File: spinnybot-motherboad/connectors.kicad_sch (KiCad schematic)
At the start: 9 parts, among them J10 LEDSTRIP3, J11 MOTOR2, J12 MOTOR3, J13 MOTOR1, J5 LEDSTRIP1, J6 LEDSTRIP2, J7 LEDSTRIP3, J8 LEDSTRIP1, J9 LEDSTRIP2

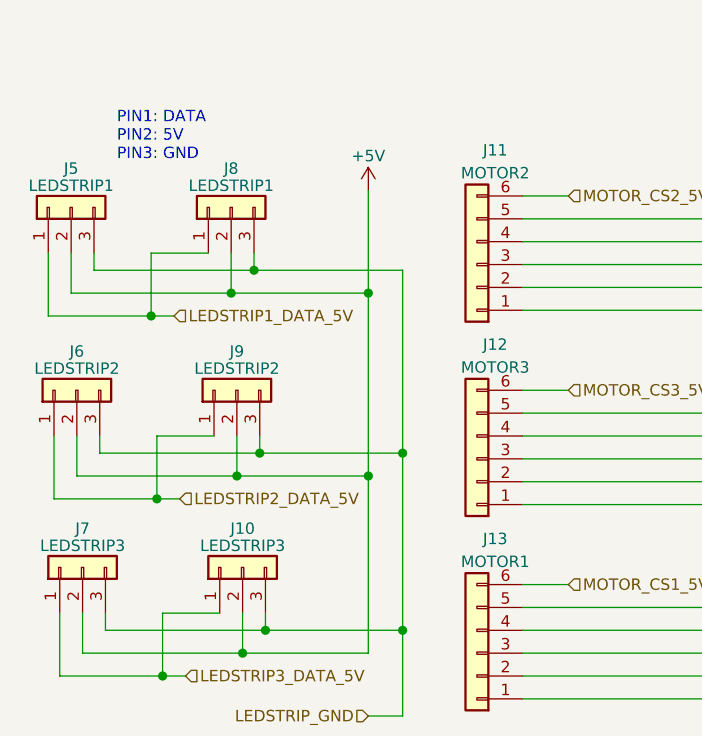
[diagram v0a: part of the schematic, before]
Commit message: fixed some reference designators so the layout isn't broken
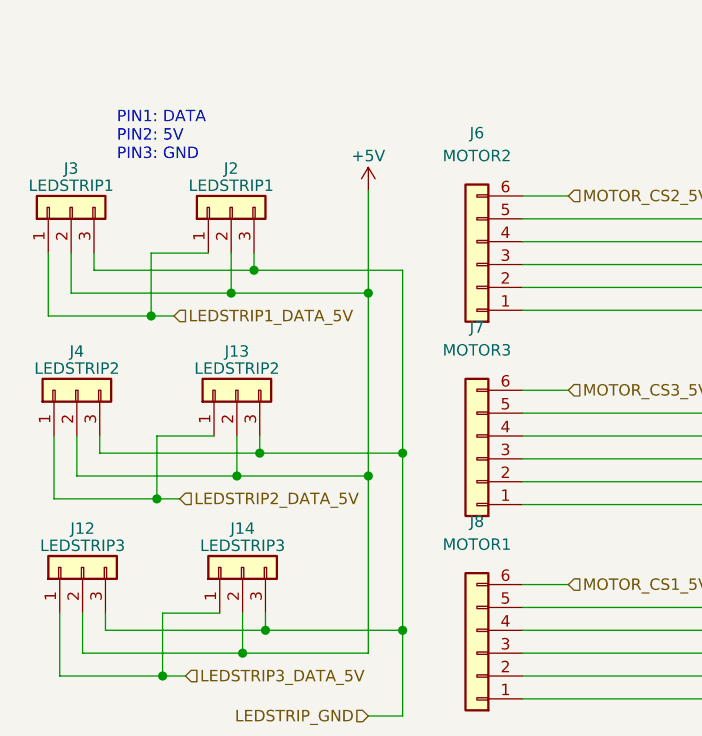
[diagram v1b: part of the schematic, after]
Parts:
- renumbered J7 to J12, J9 to J13, J10 to J14, J8 to J2, J5 to J3, J6 to J4, J11 to J6, J12 to J7, J13 to J8
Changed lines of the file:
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@@
   (symbol (lib_id "Connector_Generic:Conn_01x06") (at 144.145 114.935 180) (unit 1)
     (in_bom yes) (on_board yes) (fields_autoplaced)
-    (property "Reference" "J13" (id 0) (at 146.177 102.235 0))
-    (property "Value" "MOTOR1" (id 1) (at 146.177 104.775 0))
+    (property "Reference" "J8" (id 0) (at 144.145 100.33 0))
+    (property "Value" "MOTOR1" (id 1) (at 144.145 102.87 0))
     (property "Footprint" "S6B-XH-SM4-TB:S6B-XH-SM4-TBLFSN" (id 2) (at 144.145 114.935 0)
       (effects (font (size 1.27 1.27)) hide)
@@
   (symbol (lib_id "Connector_Generic:Conn_01x03") (at 99.695 85.725 90) (unit 1)
     (in_bom yes) (on_board yes)
-    (property "Reference" "J6" (id 0) (at 99.695 81.407 90))
+    (property "Reference" "J4" (id 0) (at 99.695 81.407 90))
     (property "Value" "LEDSTRIP2" (id 1) (at 99.695 83.312 90))
     (property "Footprint" "B3B-PH-SM4:JST_B3B-PH-SM4-TB(LF)(SN)" (id 2) (at 99.695 85.725 0)
@@
   (symbol (lib_id "Connector_Generic:Conn_01x03") (at 118.11 105.41 90) (unit 1)
     (in_bom yes) (on_board yes)
-    (property "Reference" "J10" (id 0) (at 118.11 101.092 90))
+    (property "Reference" "J14" (id 0) (at 118.11 101.092 90))
     (property "Value" "LEDSTRIP3" (id 1) (at 118.11 102.997 90))
     (property "Footprint" "B3B-PH-SM4:JST_B3B-PH-SM4-TB(LF)(SN)" (id 2) (at 118.11 105.41 0)
@@
   (symbol (lib_id "Connector_Generic:Conn_01x06") (at 144.145 71.755 180) (unit 1)
     (in_bom yes) (on_board yes) (fields_autoplaced)
-    (property "Reference" "J11" (id 0) (at 146.177 59.055 0))
-    (property "Value" "MOTOR2" (id 1) (at 146.177 61.595 0))
+    (property "Reference" "J6" (id 0) (at 144.145 57.15 0))
+    (property "Value" "MOTOR2" (id 1) (at 144.145 59.69 0))
     (property "Footprint" "S6B-XH-SM4-TB:S6B-XH-SM4-TBLFSN" (id 2) (at 144.145 71.755 0)
       (effects (font (size 1.27 1.27)) hide)
@@
   (symbol (lib_id "Connector_Generic:Conn_01x06") (at 144.145 93.345 180) (unit 1)
     (in_bom yes) (on_board yes) (fields_autoplaced)
-    (property "Reference" "J12" (id 0) (at 146.177 80.645 0))
-    (property "Value" "MOTOR3" (id 1) (at 146.177 83.185 0))
+    (property "Reference" "J7" (id 0) (at 144.145 78.74 0))
+    (property "Value" "MOTOR3" (id 1) (at 144.145 81.28 0))
     (property "Footprint" "S6B-XH-SM4-TB:S6B-XH-SM4-TBLFSN" (id 2) (at 144.145 93.345 0)
       (effects (font (size 1.27 1.27)) hide)
@@
   (symbol (lib_id "Connector_Generic:Conn_01x03") (at 99.06 65.405 90) (unit 1)
     (in_bom yes) (on_board yes)
-    (property "Reference" "J5" (id 0) (at 99.06 61.087 90))
+    (property "Reference" "J3" (id 0) (at 99.06 61.087 90))
     (property "Value" "LEDSTRIP1" (id 1) (at 99.06 62.992 90))
     (property "Footprint" "B3B-PH-SM4:JST_B3B-PH-SM4-TB(LF)(SN)" (id 2) (at 99.06 65.405 0)
@@
   (symbol (lib_id "Connector_Generic:Conn_01x03") (at 116.84 65.405 90) (unit 1)
     (in_bom yes) (on_board yes)
-    (property "Reference" "J8" (id 0) (at 116.84 61.087 90))
+    (property "Reference" "J2" (id 0) (at 116.84 61.087 90))
     (property "Value" "LEDSTRIP1" (id 1) (at 116.84 62.992 90))
     (property "Footprint" "B3B-PH-SM4:JST_B3B-PH-SM4-TB(LF)(SN)" (id 2) (at 116.84 65.405 0)
@@
   (symbol (lib_id "Connector_Generic:Conn_01x03") (at 100.33 105.41 90) (unit 1)
     (in_bom yes) (on_board yes)
-    (property "Reference" "J7" (id 0) (at 100.33 101.092 90))
+    (property "Reference" "J12" (id 0) (at 100.33 101.092 90))
     (property "Value" "LEDSTRIP3" (id 1) (at 100.33 102.997 90))
     (property "Footprint" "B3B-PH-SM4:JST_B3B-PH-SM4-TB(LF)(SN)" (id 2) (at 100.33 105.41 0)
@@
   (symbol (lib_id "Connector_Generic:Conn_01x03") (at 117.475 85.725 90) (unit 1)
     (in_bom yes) (on_board yes)
-    (property "Reference" "J9" (id 0) (at 117.475 81.407 90))
+    (property "Reference" "J13" (id 0) (at 117.475 81.407 90))
     (property "Value" "LEDSTRIP2" (id 1) (at 117.475 83.312 90))
     (property "Footprint" "B3B-PH-SM4:JST_B3B-PH-SM4-TB(LF)(SN)" (id 2) (at 117.475 85.725 0)

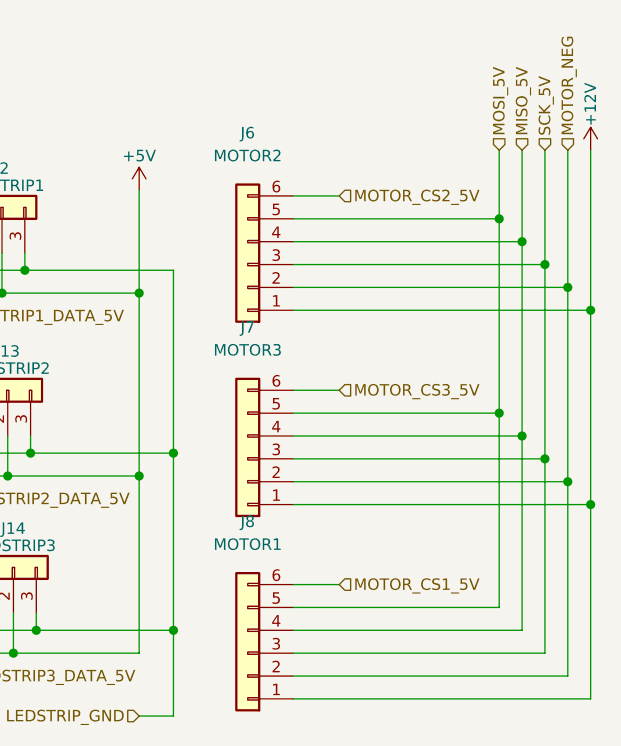
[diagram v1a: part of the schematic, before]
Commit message: Removed buck converter PS1, voltage sense divider, and motor connections. Added encoder connectors
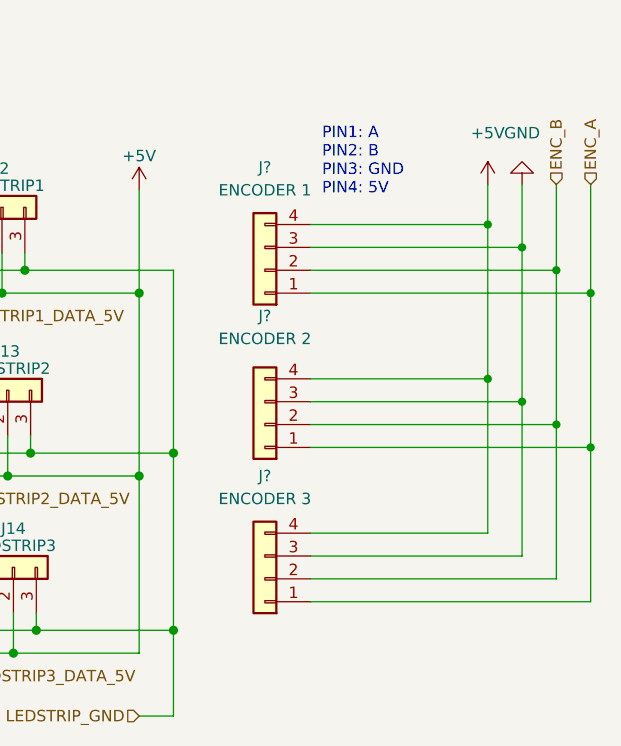
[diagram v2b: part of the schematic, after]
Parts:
- removed J6: MOTOR2, S6B-XH-SM4-TB:S6B-XH-SM4-TBLFSN, symbol Connector_Generic:Conn_01x06
- removed J7: MOTOR3, S6B-XH-SM4-TB:S6B-XH-SM4-TBLFSN, symbol Connector_Generic:Conn_01x06
- removed J8: MOTOR1, S6B-XH-SM4-TB:S6B-XH-SM4-TBLFSN, symbol Connector_Generic:Conn_01x06
- added J?: ENCODER 1, symbol Connector_Generic:Conn_01x04
- added J?: ENCODER 3, symbol Connector_Generic:Conn_01x04
- added J?: ENCODER 2, symbol Connector_Generic:Conn_01x04
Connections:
- net +5V: now also J?.4 (Pin_4), J?.4 (Pin_4), J?.4 (Pin_4)
- new net ENC_A: J?.1 (Pin_1), J?.1 (Pin_1), J?.1 (Pin_1)
- new net ENC_B: J?.2 (Pin_2), J?.2 (Pin_2), J?.2 (Pin_2)
- new net GND: J?.3 (Pin_3), J?.3 (Pin_3), J?.3 (Pin_3)
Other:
- note added: "PIN1: A PIN2: B PIN3: GND PIN4: 5V"

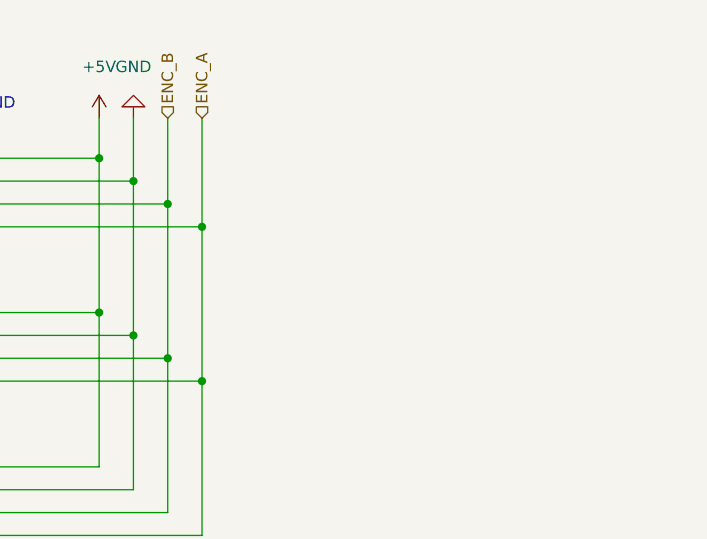
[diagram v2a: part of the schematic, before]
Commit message: Added ESC connections
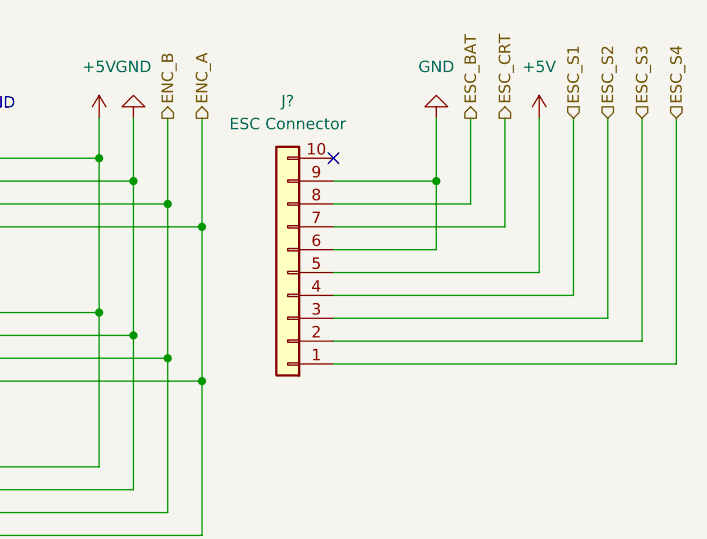
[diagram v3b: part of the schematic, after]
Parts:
- added J?: ESC Connector, symbol Connector_Generic:Conn_01x10
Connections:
- net +5V: now also J?.5 (Pin_5)
- net GND: now also J?.6 (Pin_6), J?.9 (Pin_9)
- new net ESC_BAT: J?.8 (Pin_8)
- new net ESC_CRT: J?.7 (Pin_7)
- new net ESC_S1: J?.4 (Pin_4)
- new net ESC_S2: J?.3 (Pin_3)
- new net ESC_S3: J?.2 (Pin_2)
- new net ESC_S4: J?.1 (Pin_1)
- no-connect marks 0 -> 1
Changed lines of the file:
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@@
   (junction (at 117.475 95.25) (diameter 1.016) (color 0 0 0 0)
   )
+  (junction (at 208.28 69.85) (diameter 0) (color 0 0 0 0)
+  )
   (junction (at 132.08 95.25) (diameter 1.016) (color 0 0 0 0)
   )
@@
   (junction (at 135.89 92.71) (diameter 1.016) (color 0 0 0 0)
   )
+  (no_connect (at 196.85 67.31))
   (wire (pts (xy 120.015 90.805) (xy 120.015 92.71))
     (stroke (width 0) (type solid) (color 0 0 0 0))
@@
     (stroke (width 0) (type solid) (color 0 0 0 0))
   )
+  (wire (pts (xy 212.09 72.39) (xy 196.85 72.39))
+    (stroke (width 0) (type default) (color 0 0 0 0))
+  )
   (wire (pts (xy 132.08 121.92) (xy 135.89 121.92))
     (stroke (width 0) (type solid) (color 0 0 0 0))
   )
+  (wire (pts (xy 219.71 80.01) (xy 196.85 80.01))
+    (stroke (width 0) (type default) (color 0 0 0 0))
+  )
+  (wire (pts (xy 212.09 62.865) (xy 212.09 72.39))
+    (stroke (width 0) (type default) (color 0 0 0 0))
+  )
   (wire (pts (xy 102.87 112.395) (xy 120.65 112.395))
     (stroke (width 0) (type solid) (color 0 0 0 0))
@@
     (stroke (width 0) (type default) (color 0 0 0 0))
   )
+  (wire (pts (xy 208.28 77.47) (xy 208.28 69.85))
+    (stroke (width 0) (type default) (color 0 0 0 0))
+  )
   (wire (pts (xy 108.585 97.79) (xy 108.585 90.805))
     (stroke (width 0) (type solid) (color 0 0 0 0))
@@
     (stroke (width 0) (type solid) (color 0 0 0 0))
   )
+  (wire (pts (xy 208.28 69.85) (xy 196.85 69.85))
+    (stroke (width 0) (type default) (color 0 0 0 0))
+  )
   (wire (pts (xy 132.08 114.935) (xy 118.11 114.935))
     (stroke (width 0) (type solid) (color 0 0 0 0))
@@
     (stroke (width 0) (type solid) (color 0 0 0 0))
   )
+  (wire (pts (xy 227.33 62.865) (xy 227.33 85.09))
+    (stroke (width 0) (type default) (color 0 0 0 0))
+  )
   (wire (pts (xy 182.245 109.22) (xy 182.245 92.075))
     (stroke (width 0) (type default) (color 0 0 0 0))
@@
     (stroke (width 0) (type solid) (color 0 0 0 0))
   )
+  (wire (pts (xy 234.95 90.17) (xy 196.85 90.17))
+    (stroke (width 0) (type default) (color 0 0 0 0))
+  )
   (wire (pts (xy 117.475 90.805) (xy 117.475 95.25))
     (stroke (width 0) (type solid) (color 0 0 0 0))
@@
     (stroke (width 0) (type solid) (color 0 0 0 0))
   )
+  (wire (pts (xy 223.52 62.865) (xy 223.52 82.55))
+    (stroke (width 0) (type default) (color 0 0 0 0))
+  )
   (wire (pts (xy 178.435 89.535) (xy 178.435 106.68))
     (stroke (width 0) (type default) (color 0 0 0 0))
@@
     (stroke (width 0) (type solid) (color 0 0 0 0))
   )
+  (wire (pts (xy 196.85 77.47) (xy 208.28 77.47))
+    (stroke (width 0) (type default) (color 0 0 0 0))
+  )
+  (wire (pts (xy 219.71 62.865) (xy 219.71 80.01))
+    (stroke (width 0) (type default) (color 0 0 0 0))
+  )
   (wire (pts (xy 97.155 97.79) (xy 97.155 90.805))
     (stroke (width 0) (type solid) (color 0 0 0 0))
@@
     (stroke (width 0) (type solid) (color 0 0 0 0))
   )
+  (wire (pts (xy 231.14 62.865) (xy 231.14 87.63))
+    (stroke (width 0) (type default) (color 0 0 0 0))
+  )
   (wire (pts (xy 99.695 95.25) (xy 99.695 90.805))
     (stroke (width 0) (type solid) (color 0 0 0 0))
@@
     (stroke (width 0) (type solid) (color 0 0 0 0))
   )
+  (wire (pts (xy 231.14 87.63) (xy 196.85 87.63))
+    (stroke (width 0) (type default) (color 0 0 0 0))
+  )
+  (wire (pts (xy 223.52 82.55) (xy 196.85 82.55))
+    (stroke (width 0) (type default) (color 0 0 0 0))
+  )
   (wire (pts (xy 99.06 74.93) (xy 99.06 70.485))
     (stroke (width 0) (type solid) (color 0 0 0 0))
@@
     (stroke (width 0) (type solid) (color 0 0 0 0))
   )
+  (wire (pts (xy 227.33 85.09) (xy 196.85 85.09))
+    (stroke (width 0) (type default) (color 0 0 0 0))
+  )
   (wire (pts (xy 120.65 110.49) (xy 120.65 112.395))
     (stroke (width 0) (type solid) (color 0 0 0 0))
@@
     (stroke (width 0) (type default) (color 0 0 0 0))
   )
+  (wire (pts (xy 234.95 62.865) (xy 234.95 90.17))
+    (stroke (width 0) (type default) (color 0 0 0 0))
+  )
+  (wire (pts (xy 208.28 62.865) (xy 208.28 69.85))
+    (stroke (width 0) (type default) (color 0 0 0 0))
+  )
   (wire (pts (xy 100.33 114.935) (xy 100.33 110.49))
     (stroke (width 0) (type solid) (color 0 0 0 0))
@@
     (stroke (width 0) (type solid) (color 0 0 0 0))
   )
+  (wire (pts (xy 215.9 74.93) (xy 196.85 74.93))
+    (stroke (width 0) (type default) (color 0 0 0 0))
+  )
   (wire (pts (xy 119.38 70.485) (xy 119.38 72.39))
     (stroke (width 0) (type solid) (color 0 0 0 0))
+  )
+  (wire (pts (xy 215.9 62.865) (xy 215.9 74.93))
+    (stroke (width 0) (type default) (color 0 0 0 0))
   )
   (wire (pts (xy 174.625 69.85) (xy 174.625 62.865))
@@
     (effects (font (size 1.27 1.27)) (justify right))
   )
-  (hierarchical_label "ENC_A" (shape input) (at 182.245 62.865 90)
+  (hierarchical_label "ESC_S1" (shape input) (at 223.52 62.865 90)
+    (effects (font (size 1.27 1.27)) (justify left))
+  )
+  (hierarchical_label "ENC_A" (shape output) (at 182.245 62.865 90)
     (effects (font (size 1.27 1.27)) (justify left))
   )
@@
     (effects (font (size 1.27 1.27)) (justify left))
   )
-  (hierarchical_label "ENC_B" (shape input) (at 178.435 62.865 90)
+  (hierarchical_label "ESC_CRT" (shape output) (at 215.9 62.865 90)
+    (effects (font (size 1.27 1.27)) (justify left))
+  )
+  (hierarchical_label "ENC_B" (shape output) (at 178.435 62.865 90)
     (effects (font (size 1.27 1.27)) (justify left))
   )
   (hierarchical_label "LEDSTRIP1_DATA_5V" (shape input) (at 110.49 77.47 0)
+    (effects (font (size 1.27 1.27)) (justify left))
+  )
+  (hierarchical_label "ESC_S4" (shape input) (at 234.95 62.865 90)
+    (effects (font (size 1.27 1.27)) (justify left))
+  )
+  (hierarchical_label "ESC_S3" (shape input) (at 231.14 62.865 90)
+    (effects (font (size 1.27 1.27)) (justify left))
+  )
+  (hierarchical_label "ESC_S2" (shape input) (at 227.33 62.865 90)
+    (effects (font (size 1.27 1.27)) (justify left))
+  )
+  (hierarchical_label "ESC_BAT" (shape output) (at 212.09 62.865 90)
     (effects (font (size 1.27 1.27)) (justify left))
   )
@@
     (pin "4")
   )
+  (symbol (lib_id "power:GND") (at 208.28 62.865 180) (unit 1)
+    (in_bom yes) (on_board yes) (fields_autoplaced)
+    (property "Reference" "#PWR?" (id 0) (at 208.28 56.515 0)
+      (effects (font (size 1.27 1.27)) hide)
+    )
+    (property "Value" "GND" (id 1) (at 208.28 57.15 0))
+    (property "Footprint" "" (id 2) (at 208.28 62.865 0)
+      (effects (font (size 1.27 1.27)) hide)
+    )
+    (property "Datasheet" "" (id 3) (at 208.28 62.865 0)
+      (effects (font (size 1.27 1.27)) hide)
+    )
+    (pin "1")
+  )
   (symbol (lib_id "Connector_Generic:Conn_01x04") (at 146.05 106.68 180) (unit 1)
     (in_bom yes) (on_board yes) (fields_autoplaced)
@@
     (pin "4")
   )
+  (symbol (lib_id "power:+5V") (at 219.71 62.865 0) (unit 1)
+    (in_bom yes) (on_board yes) (fields_autoplaced)
+    (property "Reference" "#PWR?" (id 0) (at 219.71 66.675 0)
+      (effects (font (size 1.27 1.27)) hide)
+    )
+    (property "Value" "+5V" (id 1) (at 219.71 57.15 0))
+    (property "Footprint" "" (id 2) (at 219.71 62.865 0)
+      (effects (font (size 1.27 1.27)) hide)
+    )
+    (property "Datasheet" "" (id 3) (at 219.71 62.865 0)
+      (effects (font (size 1.27 1.27)) hide)
+    )
+    (pin "1")
+  )
   (symbol (lib_id "Connector_Generic:Conn_01x03") (at 99.695 85.725 90) (unit 1)
     (in_bom yes) (on_board yes)
@@
     (pin "3")
   )
+  (symbol (lib_id "Connector_Generic:Conn_01x10") (at 191.77 80.01 180) (unit 1)
+    (in_bom yes) (on_board yes) (fields_autoplaced)
+    (property "Reference" "J?" (id 0) (at 191.77 60.96 0))
+    (property "Value" "ESC Connector" (id 1) (at 191.77 63.5 0))
+    (property "Footprint" "" (id 2) (at 191.77 80.01 0)
+      (effects (font (size 1.27 1.27)) hide)
+    )
+    (property "Datasheet" "~" (id 3) (at 191.77 80.01 0)
+      (effects (font (size 1.27 1.27)) hide)
+    )
+    (pin "1")
+    (pin "10")
+    (pin "2")
+    (pin "3")
+    (pin "4")
+    (pin "5")
+    (pin "6")
+    (pin "7")
+    (pin "8")
+    (pin "9")
+  )
 )

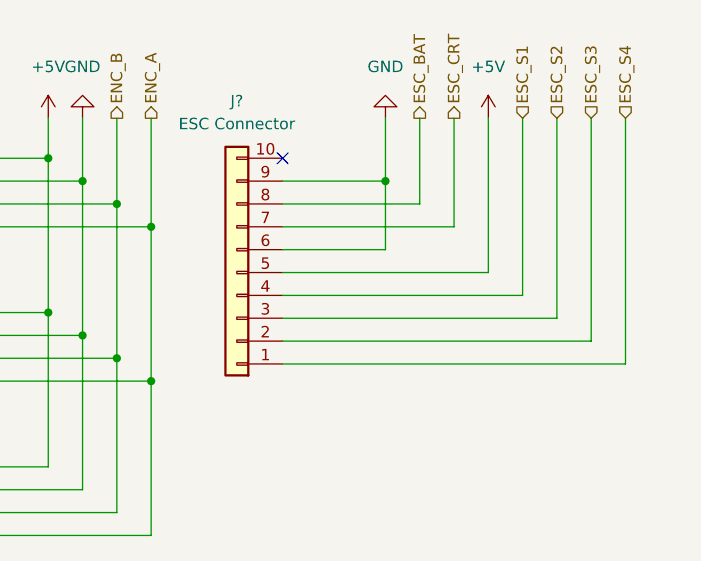
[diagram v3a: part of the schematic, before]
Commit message: Made and imported ESC footprint, added 10 pin JST connector symbol and footprint, updated Q2 FET to control ESC power
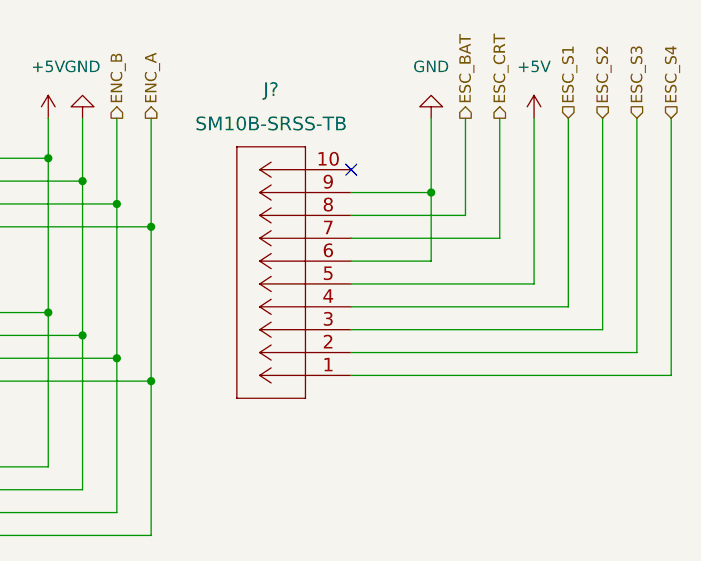
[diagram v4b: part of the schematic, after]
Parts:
- removed J?: ESC Connector, symbol Connector_Generic:Conn_01x10
- added J?: SM10B-SRSS-TB, CONN_SM10B-SRSS-TB_JST, symbol SM10B-SRSS-TB:SM10B-SRSS-TB
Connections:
- net +5V: now also J?.5
- net ESC_BAT: now also J?.8
- net ESC_CRT: now also J?.7
- net ESC_S1: now also J?.4
- net ESC_S2: now also J?.3
- net ESC_S3: now also J?.2
- net ESC_S4: now also J?.1
- net GND: now also J?.6, J?.9
